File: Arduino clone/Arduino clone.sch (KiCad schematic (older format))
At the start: 13 parts, among them U1 DS1337_RYSA, U2 24LC1025, U3 24LC1025, U4 ATMEGA328P-AU, Y1 Crystal, Y2 Crystal

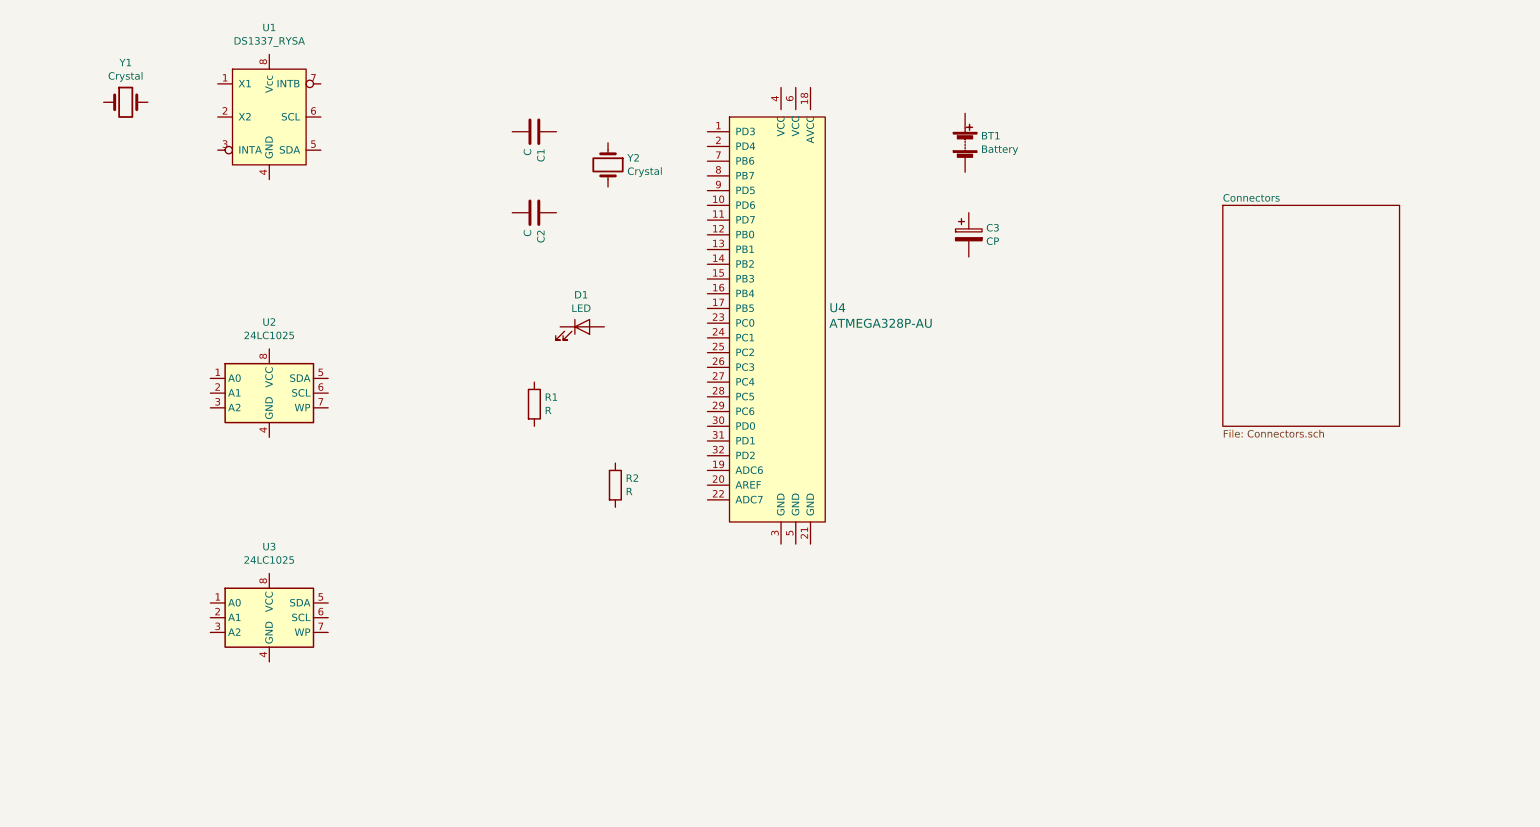
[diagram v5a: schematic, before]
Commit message: Footprints & Values
Made footprint associations and added values to symbols.
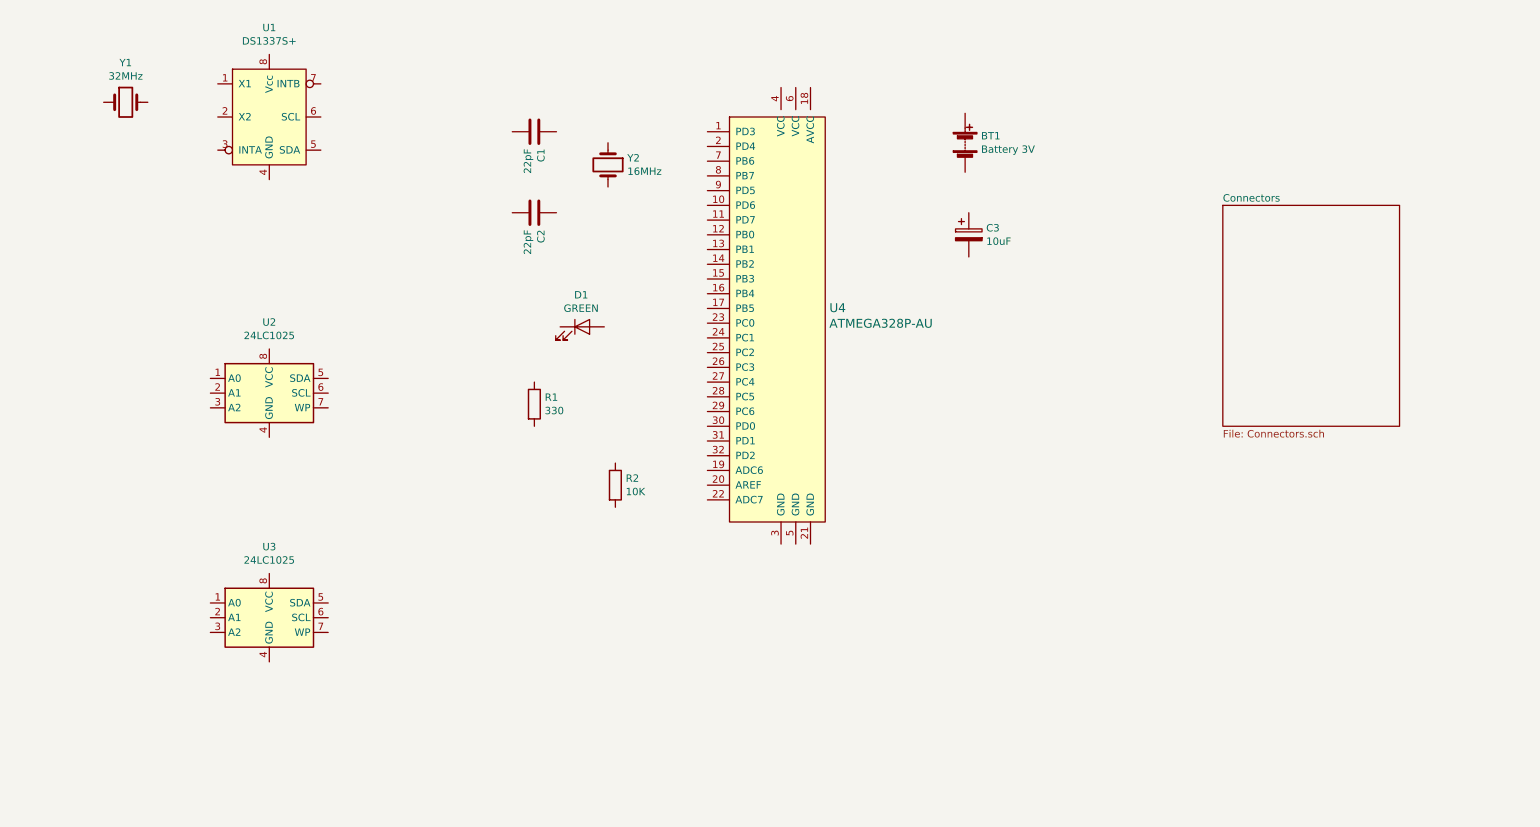
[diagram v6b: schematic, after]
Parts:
- BT1: value Battery -> Battery 3V; footprint (none) -> Connector_PinHeader_2.54mm:PinHeader_1x02_P2.54mm_Vertical
- C1, C2: value C -> 22pF; footprint (none) -> Capacitor_SMD:C_0805_2012Metric_Pad1.15x1.40mm_HandSolder
- C3: value CP -> 10uF; footprint (none) -> Capacitor_SMD:C_0805_2012Metric_Pad1.15x1.40mm_HandSolder
- D1: value LED -> GREEN; footprint (none) -> LED_SMD:LED_0805_2012Metric_Pad1.15x1.40mm_HandSolder
- R1: value R -> 330; footprint (none) -> Resistor_SMD:R_0805_2012Metric_Pad1.15x1.40mm_HandSolder
- R2: value R -> 10K; footprint (none) -> Resistor_SMD:R_0805_2012Metric_Pad1.15x1.40mm_HandSolder
- U1: value DS1337_RYSA -> DS1337S+; footprint (none) -> Package_SO:SO-8_5.3x6.2mm_P1.27mm
- U2, U3: footprint (none) -> Package_SO:SOIJ-8_5.3x5.3mm_P1.27mm
- Y1: value Crystal -> 32MHz; footprint (none) -> Crystal:Crystal_SMD_MicroCrystal_CC7V-T1A-2Pin_3.2x1.5mm
- Y2: value Crystal -> 16MHz; footprint (none) -> Crystal:Crystal_SMD_5032-2Pin_5.0x3.2mm_HandSoldering
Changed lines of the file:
@@
 P 7250 2475
 F 0 "BT1" H 7358 2521 50  0000 L CNN
-F 1 "Battery" H 7358 2430 50  0000 L CNN
-F 2 "" V 7250 2535 50  0001 C CNN
+F 1 "Battery 3V" H 7358 2430 50  0000 L CNN
+F 2 "Connector_PinHeader_2.54mm:PinHeader_1x02_P2.54mm_Vertical" V 7250 2535 50  0001 C CNN
 F 3 "~" V 7250 2535 50  0001 C CNN
 	1    7250 2475
@@
 P 4325 2400
 F 0 "C1" H 4440 2446 50  0000 L CNN
-F 1 "C" H 4440 2355 50  0000 L CNN
-F 2 "" H 4363 2250 50  0001 C CNN
+F 1 "22pF" H 4440 2355 50  0000 L CNN
+F 2 "Capacitor_SMD:C_0805_2012Metric_Pad1.15x1.40mm_HandSolder" H 4363 2250 50  0001 C CNN
 F 3 "~" H 4325 2400 50  0001 C CNN
 	1    4325 2400
@@
 P 4325 2950
 F 0 "C2" H 4440 2996 50  0000 L CNN
-F 1 "C" H 4440 2905 50  0000 L CNN
-F 2 "" H 4363 2800 50  0001 C CNN
+F 1 "22pF" H 4440 2905 50  0000 L CNN
+F 2 "Capacitor_SMD:C_0805_2012Metric_Pad1.15x1.40mm_HandSolder" H 4363 2800 50  0001 C CNN
 F 3 "~" H 4325 2950 50  0001 C CNN
 	1    4325 2950
@@
 P 7275 3100
 F 0 "C3" H 7393 3146 50  0000 L CNN
-F 1 "CP" H 7393 3055 50  0000 L CNN
-F 2 "" H 7313 2950 50  0001 C CNN
+F 1 "10uF" H 7393 3055 50  0000 L CNN
+F 2 "Capacitor_SMD:C_0805_2012Metric_Pad1.15x1.40mm_HandSolder" H 7313 2950 50  0001 C CNN
 F 3 "~" H 7275 3100 50  0001 C CNN
 	1    7275 3100
@@
 P 4650 3725
 F 0 "D1" H 4643 3941 50  0000 C CNN
-F 1 "LED" H 4643 3850 50  0000 C CNN
-F 2 "" H 4650 3725 50  0001 C CNN
+F 1 "GREEN" H 4643 3850 50  0000 C CNN
+F 2 "LED_SMD:LED_0805_2012Metric_Pad1.15x1.40mm_HandSolder" H 4650 3725 50  0001 C CNN
 F 3 "~" H 4650 3725 50  0001 C CNN
 	1    4650 3725
@@
 P 4875 4800
 F 0 "R2" H 4945 4846 50  0000 L CNN
-F 1 "R" H 4945 4755 50  0000 L CNN
-F 2 "" V 4805 4800 50  0001 C CNN
+F 1 "10K" H 4945 4755 50  0000 L CNN
+F 2 "Resistor_SMD:R_0805_2012Metric_Pad1.15x1.40mm_HandSolder" V 4805 4800 50  0001 C CNN
 F 3 "~" H 4875 4800 50  0001 C CNN
 	1    4875 4800
@@
 P 4325 4250
 F 0 "R1" H 4395 4296 50  0000 L CNN
-F 1 "R" H 4395 4205 50  0000 L CNN
-F 2 "" V 4255 4250 50  0001 C CNN
+F 1 "330" H 4395 4205 50  0000 L CNN
+F 2 "Resistor_SMD:R_0805_2012Metric_Pad1.15x1.40mm_HandSolder" V 4255 4250 50  0001 C CNN
 F 3 "~" H 4325 4250 50  0001 C CNN
 	1    4325 4250
@@
 F 0 "U2" H 2525 4656 50  0000 C CNN
 F 1 "24LC1025" H 2525 4565 50  0000 C CNN
-F 2 "" H 2525 4175 50  0001 C CNN
+F 2 "Package_SO:SOIJ-8_5.3x5.3mm_P1.27mm" H 2525 4175 50  0001 C CNN
 F 3 "http://ww1.microchip.com/downloads/en/DeviceDoc/21941B.pdf" H 2525 4175 50  0001 C CNN
 	1    2525 4175
@@
 F 0 "U3" H 2525 6181 50  0000 C CNN
 F 1 "24LC1025" H 2525 6090 50  0000 C CNN
-F 2 "" H 2525 5700 50  0001 C CNN
+F 2 "Package_SO:SOIJ-8_5.3x5.3mm_P1.27mm" H 2525 5700 50  0001 C CNN
 F 3 "http://ww1.microchip.com/downloads/en/DeviceDoc/21941B.pdf" H 2525 5700 50  0001 C CNN
 	1    2525 5700
@@
 P 2525 2300
 F 0 "U1" H 2525 2906 50  0000 C CNN
-F 1 "DS1337_RYSA" H 2525 2815 50  0000 C CNN
-F 2 "" H 2525 2300 50  0001 C CNN
+F 1 "DS1337S+" H 2525 2815 50  0000 C CNN
+F 2 "Package_SO:SO-8_5.3x6.2mm_P1.27mm" H 2525 2300 50  0001 C CNN
 F 3 "" H 2525 2300 50  0001 C CNN
 	1    2525 2300
@@
 P 1550 2200
 F 0 "Y1" H 1550 2468 50  0000 C CNN
-F 1 "Crystal" H 1550 2377 50  0000 C CNN
-F 2 "" H 1550 2200 50  0001 C CNN
+F 1 "32MHz" H 1550 2377 50  0000 C CNN
+F 2 "Crystal:Crystal_SMD_MicroCrystal_CC7V-T1A-2Pin_3.2x1.5mm" H 1550 2200 50  0001 C CNN
 F 3 "~" H 1550 2200 50  0001 C CNN
 	1    1550 2200
@@
 P 4825 2625
 F 0 "Y2" V 4779 2756 50  0000 L CNN
-F 1 "Crystal" V 4870 2756 50  0000 L CNN
-F 2 "" H 4825 2625 50  0001 C CNN
+F 1 "16MHz" V 4870 2756 50  0000 L CNN
+F 2 "Crystal:Crystal_SMD_5032-2Pin_5.0x3.2mm_HandSoldering" H 4825 2625 50  0001 C CNN
 F 3 "~" H 4825 2625 50  0001 C CNN
 	1    4825 2625

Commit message: Wiring
Made the wiring of the schematic.
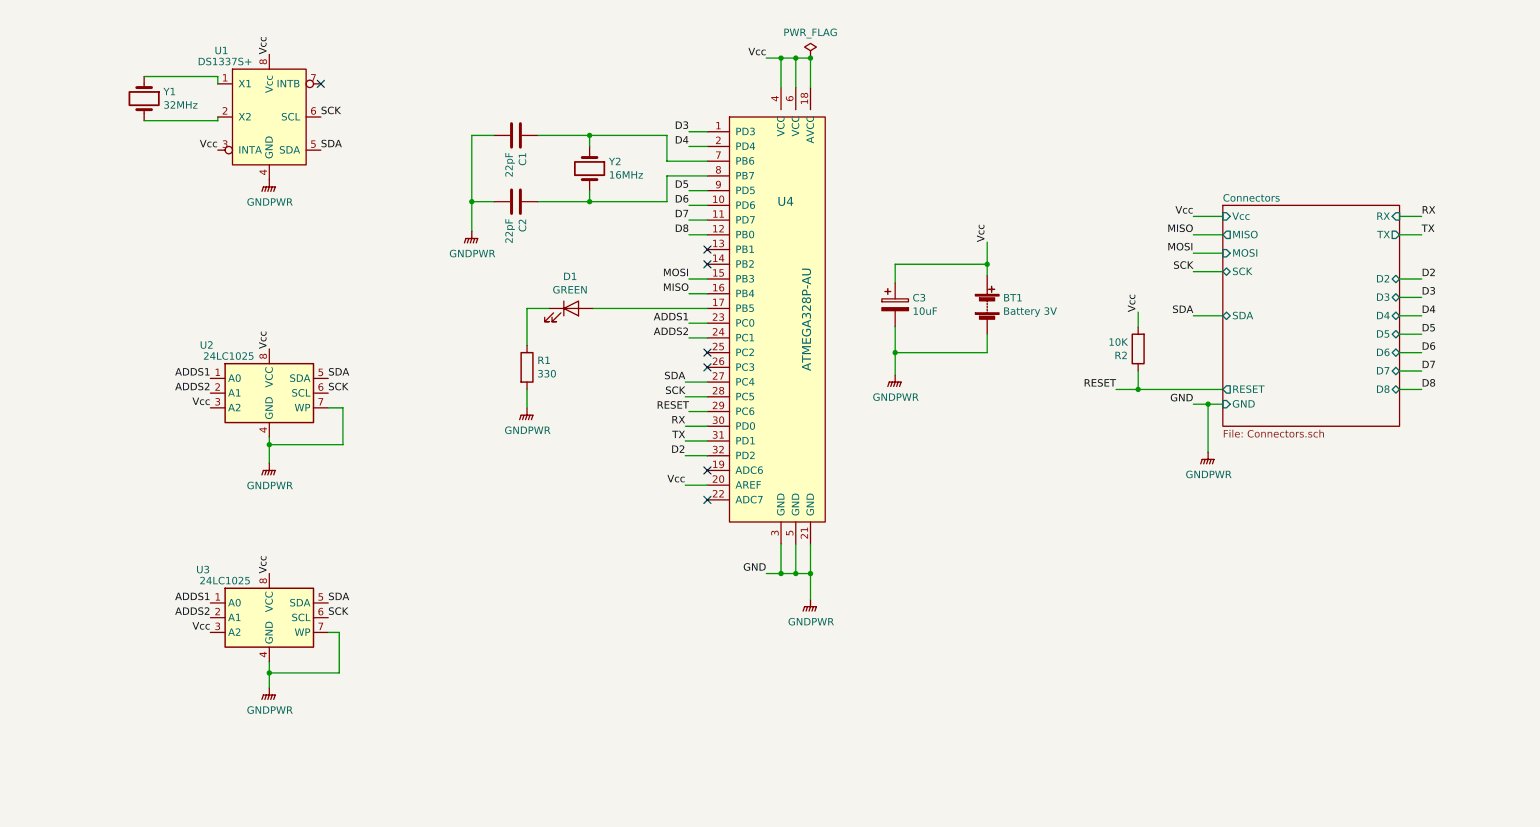
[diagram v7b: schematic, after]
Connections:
- net Vcc: now reaches BT1.1 (+)
- net Vcc: now also C3.1, R2.2, U1.3 (INTA), U1.8 (Vcc), U2.3 (A2), U2.8 (VCC), U3.3 (A2), U3.8 (VCC), U4.18 (AVCC), U4.20 (AREF), U4.4 (VCC), U4.6 (VCC)
- net GNDPWR: now reaches BT1.2 (-)
- net GNDPWR: now also C1.2, C2.2, C3.2, R1.2, U1.4 (GND), U2.4 (GND), U2.7 (WP), U3.4 (GND), U3.7 (WP), U4.21 (GND), U4.3 (GND), U4.5 (GND)
- net at C1.1: now also U4.7 (PB6), Y2.1
- net at C2.1: now also U4.8 (PB7), Y2.2
- net at D1.1 (K): now also R1.1
- net at D1.2 (A): now also U4.17 (PB5)
- net RESET: now reaches R2.1
- net RESET: now also U4.29 (PC6)
- net ADDS1: now reaches U2.1 (A0)
- net ADDS1: now also U3.1 (A0), U4.23 (PC0)
- net ADDS2: now reaches U2.2 (A1)
- net ADDS2: now also U3.2 (A1), U4.24 (PC1)
- net SDA: now reaches U2.5 (SDA)
- net SDA: now also U1.5 (SDA), U3.5 (SDA), U4.27 (PC4)
- net SCK: now reaches U2.6 (SCL)
- net SCK: now also U1.6 (SCL), U3.6 (SCL), U4.28 (PC5)
- net D3: now reaches U4.1 (PD3)
- net D6: now reaches U4.10 (PD6)
- net D7: now reaches U4.11 (PD7)
- net D8: now reaches U4.12 (PB0)
- net MOSI: now reaches U4.15 (PB3)
- net MISO: now reaches U4.16 (PB4)
- net D4: now reaches U4.2 (PD4)
- net RX: now reaches U4.30 (PD0)
- net TX: now reaches U4.31 (PD1)
- net D2: now reaches U4.32 (PD2)
- net D5: now reaches U4.9 (PD5)
- net at U1.1 (X1): now also Y1.1
- net at U1.2 (X2): now also Y1.2
- no-connect marks 0 -> 7
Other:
- moved on the sheet: BT1, C1, C2, C3, D1, R1, R2, Y1, Y2

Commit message: Comments
Added block comments.
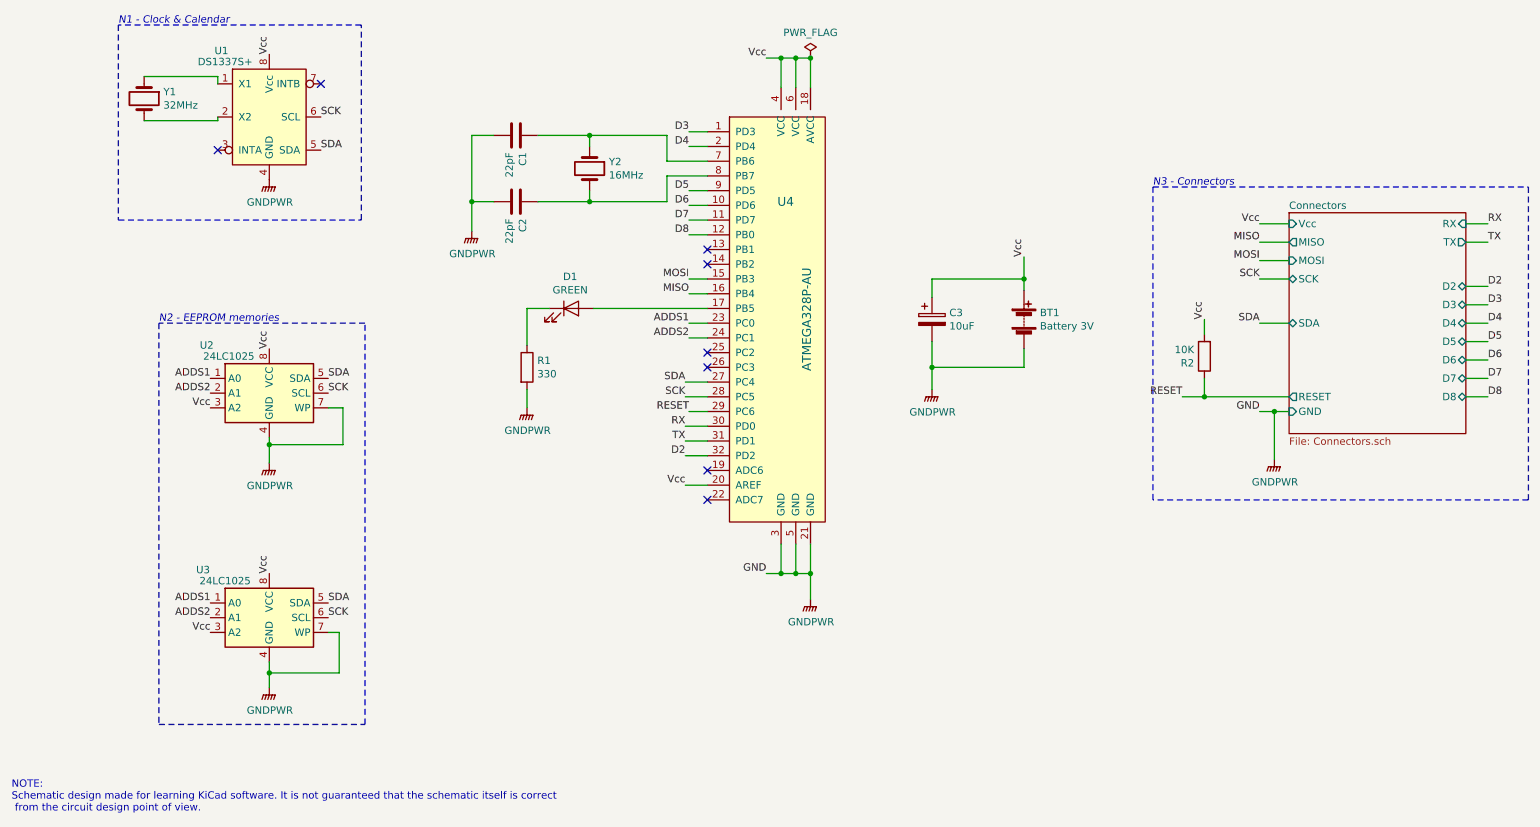
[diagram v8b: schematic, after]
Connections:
- net Vcc: no longer U1.3 (INTA)
- no-connect marks 7 -> 8
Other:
- note added: "N1 - Clock & Calendar"
- note added: "N2 - EEPROM memories"
- note added: "N3 - Connectors"
- note added: "NOTE:\nSchematic design made for learning KiCad software. It is not guaranteed that the schematic itself is correct\n from the circuit design point of view."
- moved on the sheet: BT1, C3, R2
